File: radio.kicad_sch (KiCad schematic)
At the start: 2 parts, among them J4 Conn_Coaxial, U4 RFM95W-915S2

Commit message: update schematics and add 3d models
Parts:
- J4: footprint Connector_Coaxial:U.FL_Molex_MCRF_73412-0110_Vertical -> Connector_Coaxial:U.FL_Hirose_U.FL-R-SMT-1_Vertical; LCSC (none) -> C88374
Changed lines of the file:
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@@
+			)
+		)
+		(property "LCSC" ""
+			(at 119.38 85.09 0)
+			(effects
+				(font
+					(size 1.27 1.27)
+				)
+				(hide yes)
 			)
 		)
@@
 			)
 		)
-		(property "Footprint" "Connector_Coaxial:U.FL_Molex_MCRF_73412-0110_Vertical"
+		(property "Footprint" "Connector_Coaxial:U.FL_Hirose_U.FL-R-SMT-1_Vertical"
 			(at 151.13 77.47 0)
 			(effects
@@
 			(at 151.13 77.47 0)
 			(effects
+				(font
+					(size 1.27 1.27)
+				)
+				(hide yes)
+			)
+		)
+		(property "LCSC" "C88374"
+			(at 151.13 77.47 0)
+			(effects

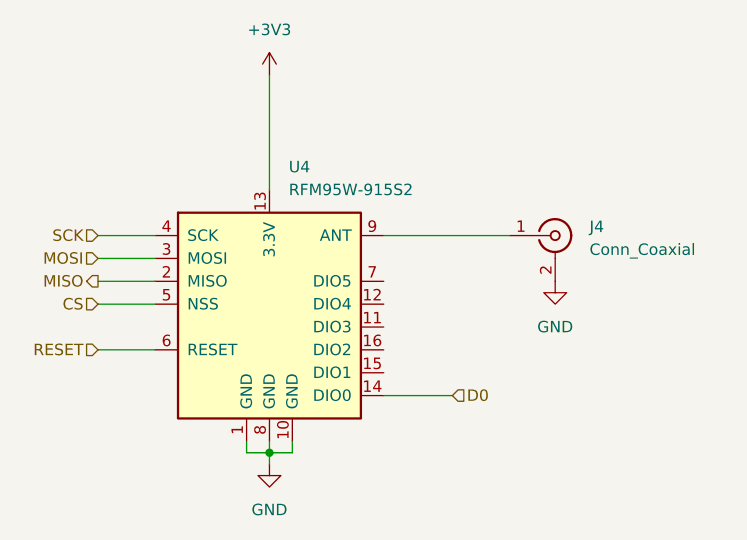
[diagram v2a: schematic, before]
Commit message: finished power, checked most sensor schematics
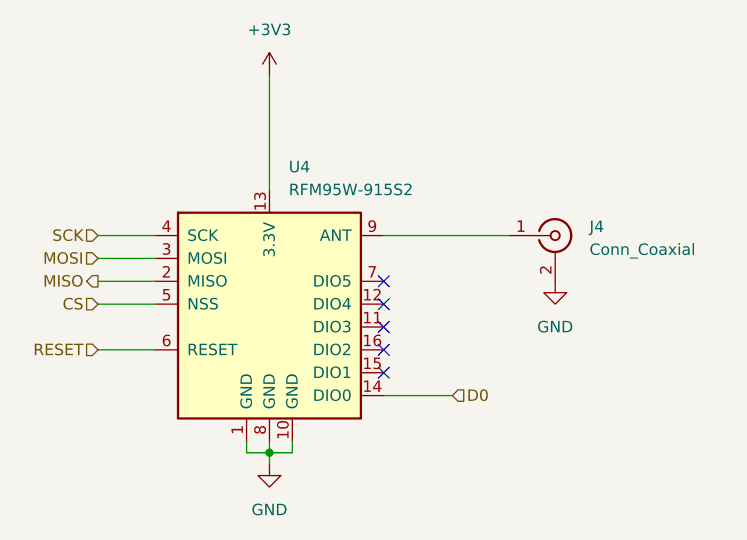
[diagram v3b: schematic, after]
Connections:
- no-connect marks 0 -> 5
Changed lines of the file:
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@@
 		(color 0 0 0 0)
+	)
+	(no_connect
+		(at 132.08 82.55)
+	)
+	(no_connect
+		(at 132.08 87.63)
+	)
+	(no_connect
+		(at 132.08 90.17)
+	)
+	(no_connect
+		(at 132.08 85.09)
+	)
+	(no_connect
+		(at 132.08 92.71)
 	)
 	(wire

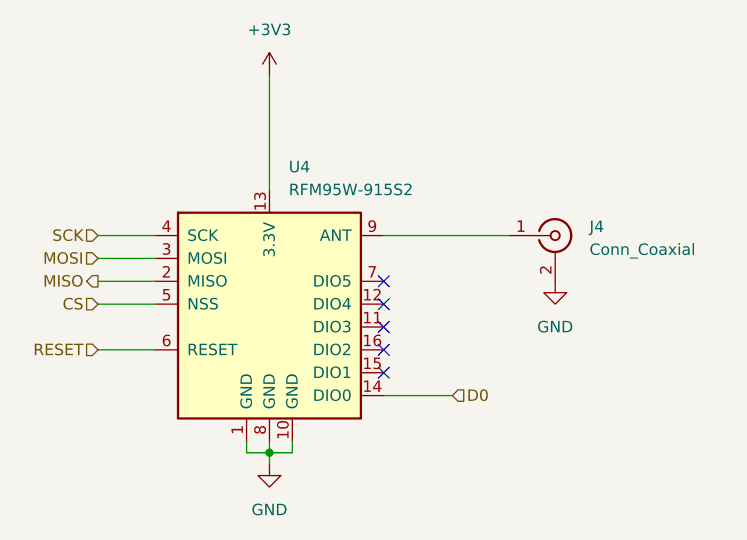
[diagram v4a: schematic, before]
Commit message: switched to global labels for SPI and I2C, added labels for servos
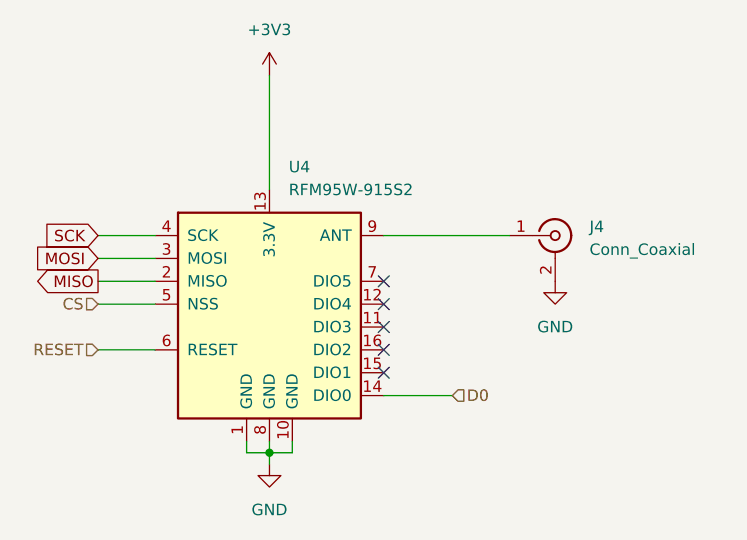
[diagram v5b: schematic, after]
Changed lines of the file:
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@@
 		)
 	)
-	(hierarchical_label "SCK"
-		(shape input)
-		(at 100.33 77.47 180)
+	(global_label "MISO"
+		(shape output)
+		(at 100.33 82.55 180)
+		(fields_autoplaced yes)
 		(effects
 			(font
@@
 			(justify right)
 		)
+		(property "Intersheetrefs" "${INTERSHEET_REFS}"
+			(at 92.7486 82.55 0)
+			(effects
+				(font
+					(size 1.27 1.27)
+				)
+				(justify right)
+				(hide yes)
+			)
+		)
 	)
-	(hierarchical_label "MOSI"
+	(global_label "MOSI"
 		(shape input)
 		(at 100.33 80.01 180)
+		(fields_autoplaced yes)
 		(effects
 			(font
@@
 			(justify right)
 		)
+		(property "Intersheetrefs" "${INTERSHEET_REFS}"
+			(at 92.7486 80.01 0)
+			(effects
+				(font
+					(size 1.27 1.27)
+				)
+				(justify right)
+				(hide yes)
+			)
+		)
 	)
-	(hierarchical_label "MISO"
-		(shape output)
-		(at 100.33 82.55 180)
+	(global_label "SCK"
+		(shape input)
+		(at 100.33 77.47 180)
+		(fields_autoplaced yes)
 		(effects
 			(font
@@
 			(justify right)
 		)
+		(property "Intersheetrefs" "${INTERSHEET_REFS}"
+			(at 93.5953 77.47 0)
+			(effects
+				(font
+					(size 1.27 1.27)
+				)
+				(justify right)
+				(hide yes)
+			)
+		)
 	)
